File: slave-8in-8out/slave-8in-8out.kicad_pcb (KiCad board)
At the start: 2 copper layers, 69.6 x 71.6 mm, 87 parts, among them J1 Conn_01x06_Male, J2 Screw_Terminal_01x02, J3 Conn_01x06_Female, J4 Screw_Terminal_01x04, J5 Screw_Terminal_01x04, J6 Screw_Terminal_01x04, J7 Screw_Terminal_01x04, J8 Conn_01x10_Female, J9 Screw_Terminal_01x02, SW1 SW_DIP_x03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

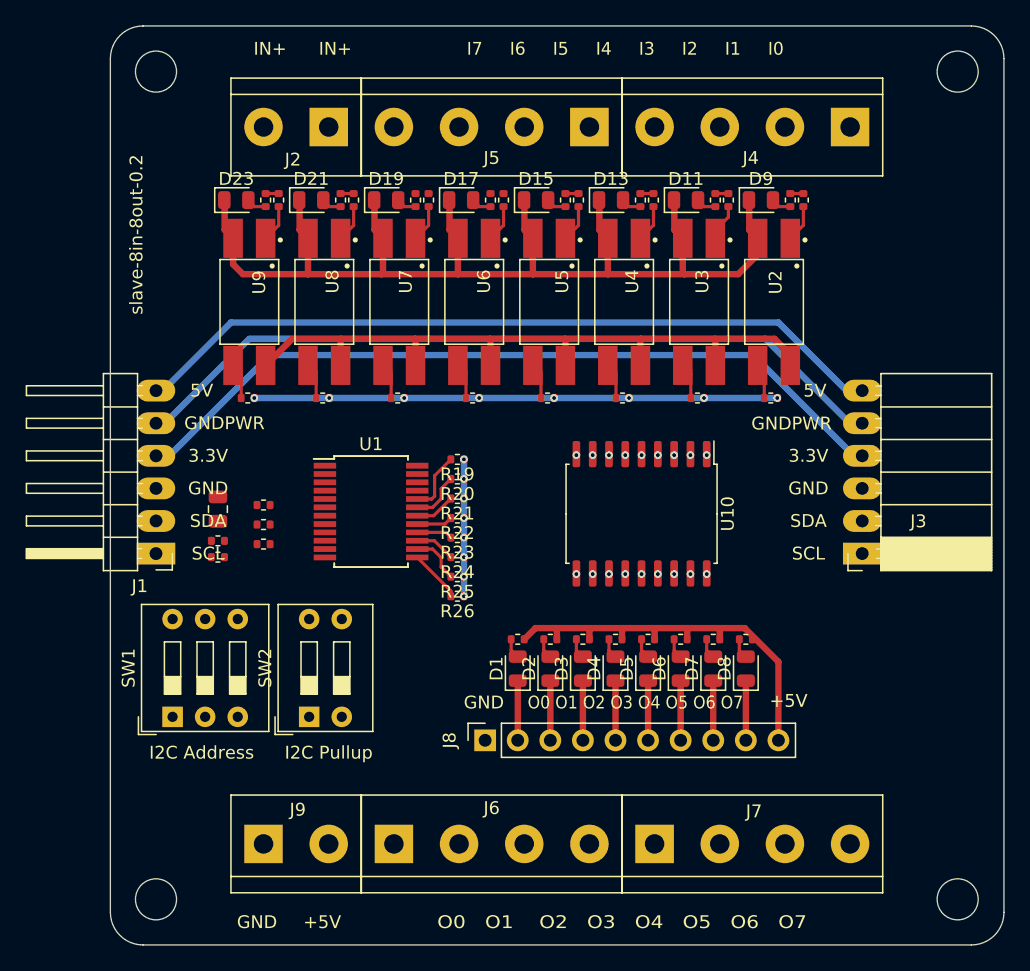
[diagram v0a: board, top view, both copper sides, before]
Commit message: update slave-8in-8out routing
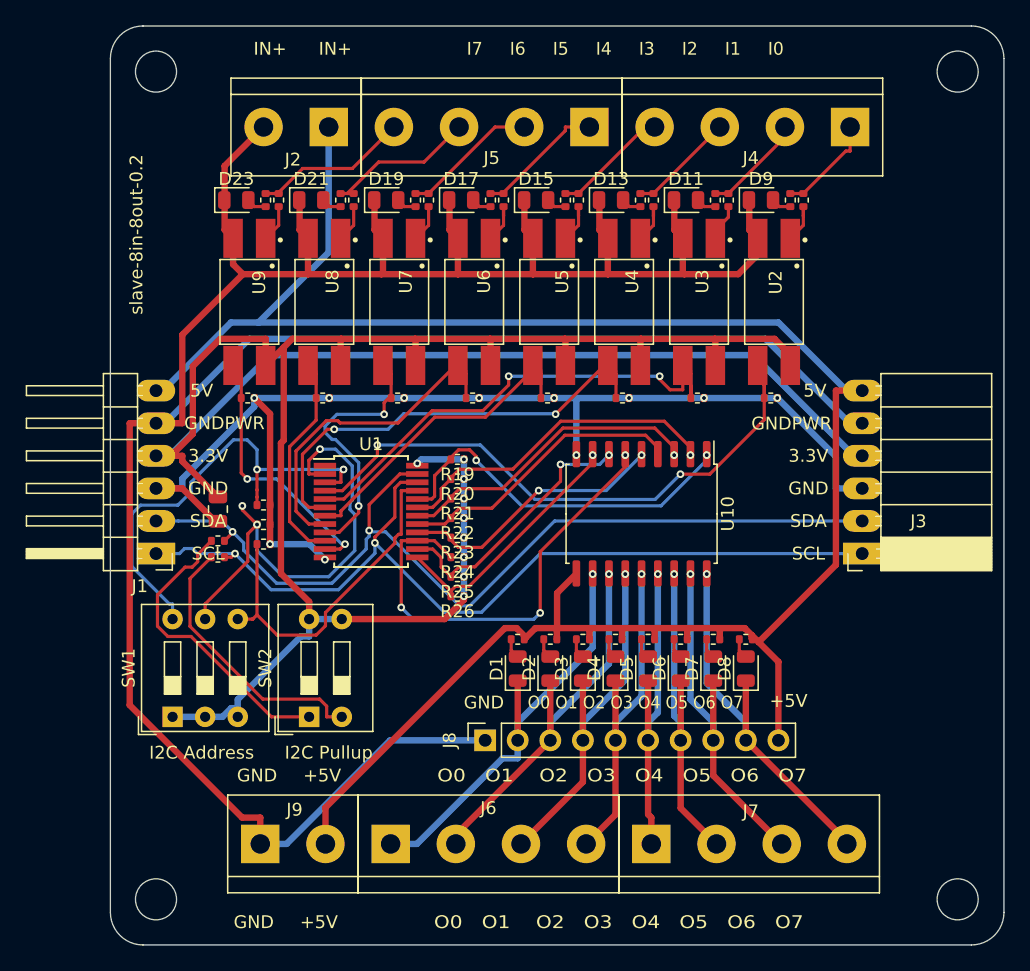
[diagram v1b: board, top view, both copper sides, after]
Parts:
- moved J6 0.25 mm to (91.4, 124.0)
- moved J9 0.25 mm to (81.3, 124.0)
- moved J7 0.25 mm to (111.8, 124.0)
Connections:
- J2 pad 2: +5V -> GNDPWR
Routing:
- net GNDPWR: track 148.6 -> 232.1 mm
- net +3V3: track 127.9 -> 208.7 mm, vias 8 -> 9
- net SDA: track 0.00 -> 72.8 mm, vias 0 -> 2
- net +5V: track 92.1 -> 163.7 mm, vias 1 -> 0
- net SCL: track 0.00 -> 70.5 mm, vias 0 -> 2
- net GND: track 40.8 -> 90.3 mm, vias 9 -> 11
- net GPB0: track 4.19 -> 48.1 mm, vias 0 -> 2
- net A2: track 0.00 -> 36.0 mm, vias 0 -> 2
- net GPB1: track 3.70 -> 39.5 mm, vias 0 -> 2
- net A1: track 0.00 -> 35.7 mm, vias 0 -> 3
- net GPA2: track 3.23 -> 36.1 mm, vias 1 -> 3
- net GPB2: track 4.42 -> 36.8 mm, vias 0 -> 2
- net O0: track 4.72 -> 34.2 mm
- net A0: track 0.00 -> 27.8 mm
- net O1: track 4.72 -> 30.7 mm
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
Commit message: update slave-8in-8out routing
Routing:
- net GPA6: vias 1 -> 0
- net GPA5: vias 1 -> 0
- net GPA2: vias 3 -> 2
- net GPA0: vias 1 -> 0

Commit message: slave-8in-8out-0.2
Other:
- board text added: "slave-8in-8out-1.0"
- board text removed: "slave-8in-8out-0.2"
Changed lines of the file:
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@@
     (effects (font (size 1 1) (thickness 0.15)))
   )
-  (gr_text "slave-8in-8out-0.2" (at 71.628 76.454 90) (layer "F.SilkS")
+  (gr_text "slave-8in-8out-1.0" (at 71.628 76.454 90) (layer "F.SilkS")
     (effects (font (size 1 1) (thickness 0.15)))
   )

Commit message: update slave-8in-8out labels
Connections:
- D1 pad 1: O0 -> O1
- D2 pad 1: O1 -> O2
- D3 pad 1: O2 -> O3
- D4 pad 1: O3 -> O4
- D5 pad 1: O4 -> O5
- D6 pad 1: O5 -> O6
- D7 pad 1: O6 -> O7
- D8 pad 1: O7 -> O8
- J4 pad 1: I0 -> I1
- J4 pad 2: I1 -> I2
- J4 pad 3: I2 -> I3
- J4 pad 4: I3 -> I4
- J5 pad 1: I4 -> I5
- J5 pad 2: I5 -> I6
- J5 pad 3: I6 -> I7
- J5 pad 4: I7 -> I8
- J6 pad 1: O0 -> O1
- J6 pad 2: O1 -> O2
- J6 pad 3: O2 -> O3
- J6 pad 4: O3 -> O4
- J7 pad 1: O4 -> O5
- J7 pad 2: O5 -> O6
- J7 pad 3: O6 -> O7
- J7 pad 4: O7 -> O8
- J8 pad 2: O0 -> O1
- J8 pad 3: O1 -> O2
- J8 pad 4: O2 -> O3
- J8 pad 5: O3 -> O4
- J8 pad 6: O4 -> O5
- J8 pad 7: O5 -> O6
- J8 pad 8: O6 -> O7
- J8 pad 9: O7 -> O8
- R10 pad 2: I2 -> I3
- R3 pad 1: I0 -> I1
- R32 pad 1: I3 -> I4
- R33 pad 2: I3 -> I4
- R35 pad 1: I4 -> I5
- R36 pad 2: I4 -> I5
- R38 pad 1: I5 -> I6
- R39 pad 2: I5 -> I6
- R4 pad 2: I0 -> I1
- R41 pad 1: I6 -> I7
- R42 pad 2: I6 -> I7
- R44 pad 1: I7 -> I8
- R45 pad 2: I7 -> I8
- R6 pad 1: I1 -> I2
- R7 pad 2: I1 -> I2
- R9 pad 1: I2 -> I3
- U10 pad 11: O0 -> O1
- U10 pad 12: O1 -> O2
- U10 pad 13: O2 -> O3
- U10 pad 14: O3 -> O4
- U10 pad 15: O4 -> O5
- U10 pad 16: O5 -> O6
- U10 pad 17: O6 -> O7
- U10 pad 18: O7 -> O8
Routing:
- net O0: track 34.2 -> 0.00 mm, vias 1 -> 0
- net O8: track 0.00 -> 30.3 mm, vias 0 -> 1
- net I8: track 0.00 -> 12.2 mm
- net I0: track 7.91 -> 0.00 mm
- net O1: track 30.7 -> 34.2 mm
- net O7: track 30.3 -> 28.7 mm
- net O3: track 27.5 -> 29.1 mm
- net O2: track 29.1 -> 30.7 mm
- net O6: track 28.7 -> 27.1 mm
- net O4: track 26.2 -> 27.5 mm
- net I6: track 11.9 -> 10.6 mm
- net I4: track 10.1 -> 9.10 mm
- net O5: track 27.1 -> 26.2 mm
- net I3: track 9.10 -> 8.34 mm
- net I5: track 10.6 -> 10.1 mm
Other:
- board text added: "I8 I7 I6 I5 I4 I3 I2 I1"
- board text added: "O1 O2 O3 O4 O5 O6 O7 O8"
- board text removed: "I7 I6 I5 I4 I3 I2 I1 I0"
- board text removed: "O0 O1 O2 O3 O4 O5 O6 O7"

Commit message: update slave-8in-8out
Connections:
- J2 pad 2: GNDPWR -> +5V
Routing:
- net GNDPWR: track 232.1 -> 225.1 mm
- net +5V: track 163.7 -> 168.8 mm
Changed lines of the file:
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@@
       (net 67 "+5V") (pinfunction "Pin_1") (pintype "passive"))
     (pad "2" thru_hole circle locked (at 5.08 0 180) (size 3 3) (drill 1.52) (layers *.Cu *.Mask)
-      (net 1 "GNDPWR") (pinfunction "Pin_2") (pintype "passive"))
+      (net 67 "+5V") (pinfunction "Pin_2") (pintype "passive"))
     (model "${KISYS3DMOD}/TerminalBlock.3dshapes/TerminalBlock_bornier-2_P5.08mm.wrl"
       (offset (xyz 2.539999962 0 0))
@@
   (segment (start 78.475 73.7675) (end 78.5 73.7675) (width 0.5) (layer "F.Cu") (net 1))
   (segment (start 101.868 73.7675) (end 101.868 76.091) (width 0.5) (layer "F.Cu") (net 1))
-  (segment (start 78.5 71.106) (end 78.5 73.7675) (width 0.5) (layer "F.Cu") (net 1))
   (segment (start 79.1585 76.7495) (end 79.1585 78.7775) (width 0.5) (layer "F.Cu") (net 1))
   (segment (start 108.3687 76.7493) (end 108.369 76.7495) (width 0.5) (layer "F.Cu") (net 1))
@@
   (segment (start 101.843 73.7675) (end 101.868 73.7675) (width 0.5) (layer "F.Cu") (net 1))
   (segment (start 102.5265 76.7495) (end 102.5267 76.7493) (width 0.5) (layer "F.Cu") (net 1))
-  (segment (start 81.534 68.072) (end 78.5 71.106) (width 0.5) (layer "F.Cu") (net 1))
   (segment (start 96.026 76.091) (end 96.6845 76.7495) (width 0.5) (layer "F.Cu") (net 1))
   (segment (start 108.369 79.5395) (end 108.373 79.5435) (width 0.5) (layer "F.Cu") (net 1))
@@
   (segment (start 86.614 77.8332) (end 81.1352 83.312) (width 0.5) (layer "B.Cu") (net 67))
   (segment (start 73.152 88.621) (end 73.685 88.621) (width 0.5) (layer "B.Cu") (net 67))
+  (segment (start 81.534 68.072) (end 86.614 68.072) (width 0.5) (layer "B.Cu") (net 67))
   (segment (start 73.685 88.621) (end 78.994 83.312) (width 0.5) (layer "B.Cu") (net 67))
   (segment (start 81.1352 83.312) (end 121.666 83.312) (width 0.5) (layer "B.Cu") (net 67))

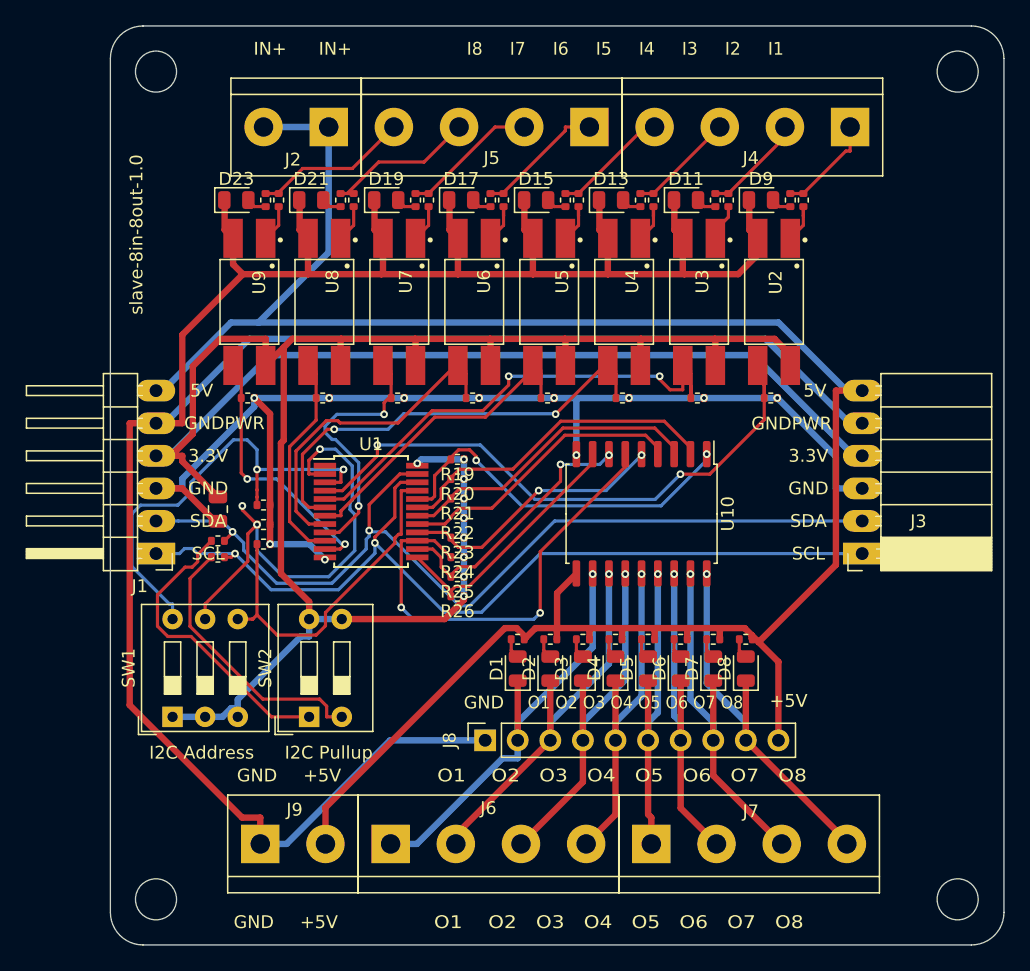
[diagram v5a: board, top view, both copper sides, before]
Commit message: fix slave-8in-8out routing
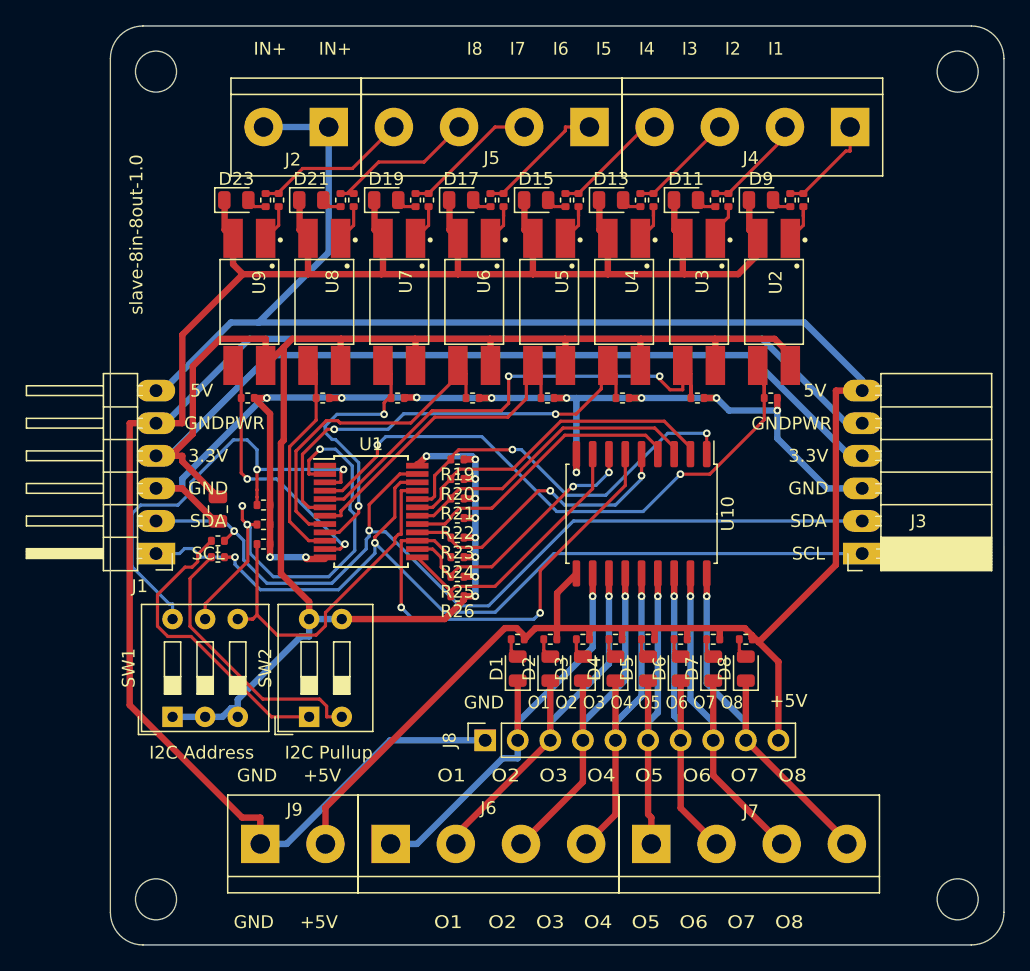
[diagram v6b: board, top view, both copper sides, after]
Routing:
- net GND: track 90.3 -> 100.9 mm
- net +3V3: track 208.7 -> 216.9 mm
- net GPA3: track 21.2 -> 23.2 mm
- net GPB0: track 48.1 -> 49.4 mm
- net GPA7: track 29.1 -> 30.3 mm
- net GPA0: track 20.0 -> 21.2 mm
- net GPB3: track 26.1 -> 27.1 mm
- net A1: track 35.7 -> 36.7 mm
- net GPB2: track 36.8 -> 37.7 mm
- net GPB1: track 39.5 -> 40.4 mm
- net SDA: track 72.8 -> 73.5 mm
- net GPB4: track 26.8 -> 27.4 mm
